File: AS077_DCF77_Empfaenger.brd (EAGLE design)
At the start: 160 x 100 mm, 82 parts, among them IC1 4093N, IC2 4538N, IC3 CA3130E, IC4 4093N, J1 Rückkopplung, J2 JUMPER_J5MM, J3 JUMPER_J5MM, Q1 BF 244A, Q2 BC549C, Q3 BC549, Q4 TRANSISTOR-NPN_BC2385.08, Q5 BC549C, Q6 TRANSISTOR-PNP_BC2145.08, Q7 BC549C

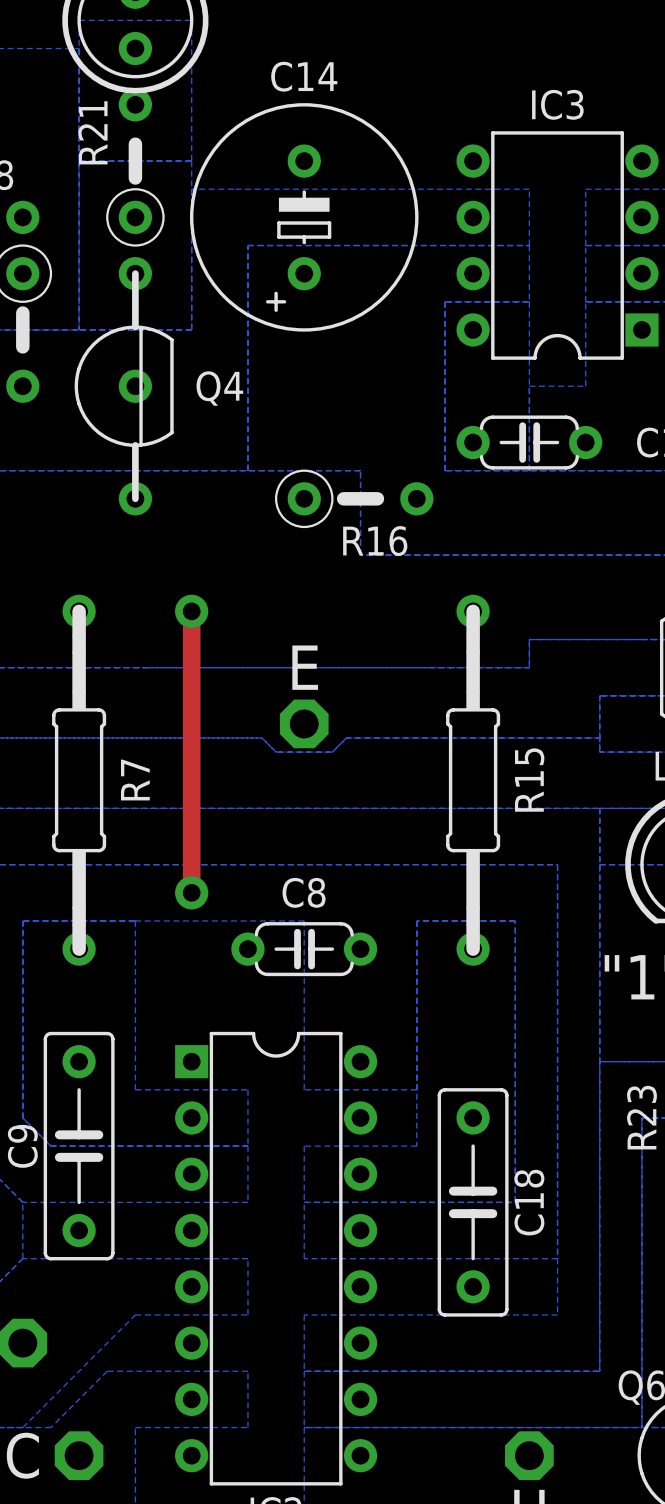
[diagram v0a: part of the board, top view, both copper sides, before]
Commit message: * Added "bottom capacitor" * Added nets and polygons to not connected IC pins
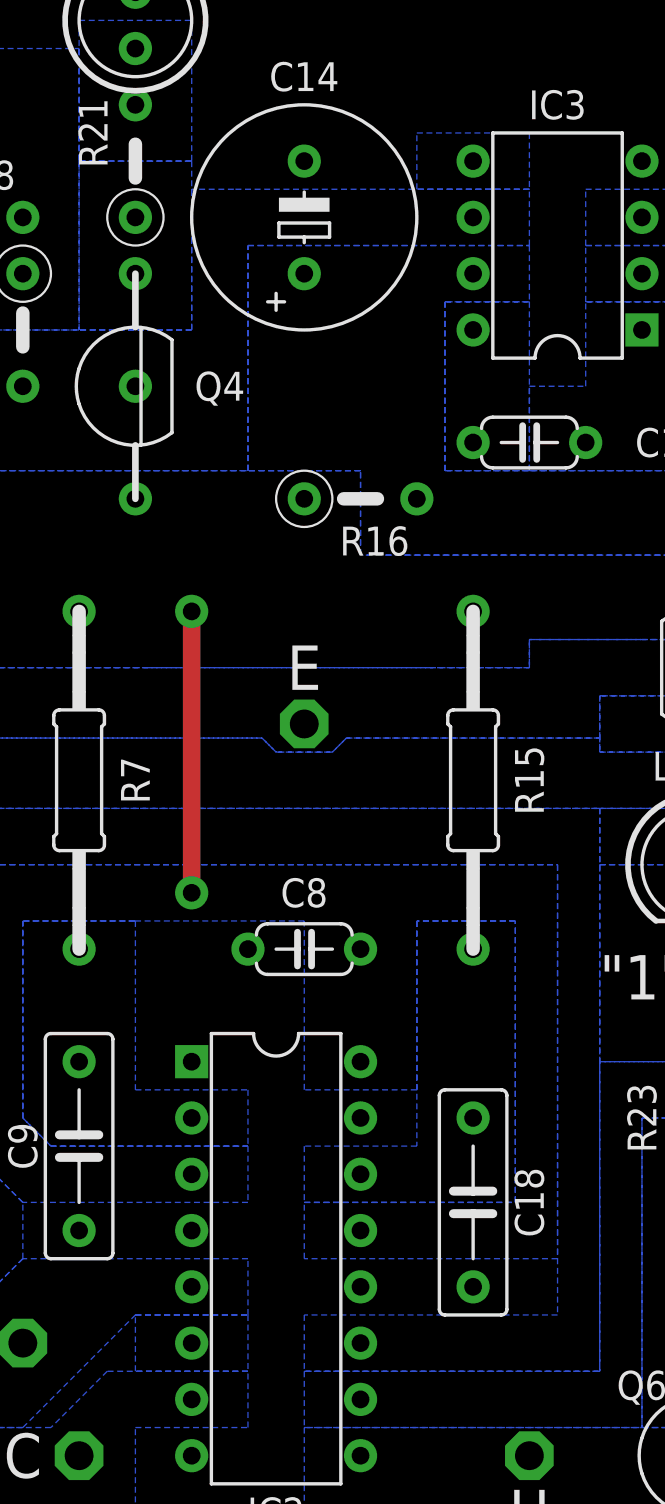
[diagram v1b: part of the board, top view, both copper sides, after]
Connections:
- new net N$45: IC2.6
- new net N$46: IC3.5
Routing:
- added copper zone on layer 16, net N$45
- added copper zone on layer 16, net N$46
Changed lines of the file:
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@@
 <layer number="37" name="tTest" color="7" fill="1" visible="no" active="yes"/>
 <layer number="38" name="bTest" color="7" fill="1" visible="no" active="yes"/>
-<layer number="39" name="tKeepout" color="4" fill="11" visible="no" active="yes"/>
-<layer number="40" name="bKeepout" color="1" fill="11" visible="no" active="yes"/>
-<layer number="41" name="tRestrict" color="4" fill="10" visible="no" active="yes"/>
-<layer number="42" name="bRestrict" color="1" fill="10" visible="no" active="yes"/>
+<layer number="39" name="tKeepout" color="4" fill="11" visible="yes" active="yes"/>
+<layer number="40" name="bKeepout" color="1" fill="11" visible="yes" active="yes"/>
+<layer number="41" name="tRestrict" color="4" fill="10" visible="yes" active="yes"/>
+<layer number="42" name="bRestrict" color="1" fill="10" visible="yes" active="yes"/>
 <layer number="43" name="vRestrict" color="2" fill="10" visible="no" active="yes"/>
 <layer number="44" name="Drills" color="7" fill="1" visible="no" active="yes"/>
-<layer number="45" name="Holes" color="7" fill="1" visible="yes" active="yes"/>
+<layer number="45" name="Holes" color="7" fill="1" visible="no" active="yes"/>
 <layer number="46" name="Milling" color="3" fill="1" visible="no" active="yes"/>
 <layer number="47" name="Measures" color="7" fill="1" visible="no" active="yes"/>
@@
 <text x="142.24" y="27.94" size="3" layer="25" font="vector" ratio="15" align="center">Piezo-
 Element</text>
+<wire x1="129.81" y1="43.815" x2="126.365" y2="43.815" width="0.5" layer="22" style="longdash"/>
+<wire x1="126.365" y1="43.815" x2="125.73" y2="43.18" width="0.5" layer="22" style="longdash" curve="90"/>
+<wire x1="125.73" y1="43.18" x2="125.73" y2="38.1" width="0.5" layer="22" style="longdash"/>
+<wire x1="125.73" y1="38.1" x2="126.365" y2="37.465" width="0.5" layer="22" style="longdash" curve="90"/>
+<wire x1="126.365" y1="37.465" x2="129.81" y2="37.465" width="0.5" layer="22" style="longdash"/>
+<wire x1="129.81" y1="37.465" x2="130.81" y2="38.465" width="0.5" layer="22" style="longdash" curve="90"/>
+<wire x1="130.81" y1="38.465" x2="130.81" y2="42.815" width="0.5" layer="22" style="longdash"/>
+<wire x1="130.81" y1="42.815" x2="129.81" y2="43.815" width="0.5" layer="22" style="longdash" curve="90"/>
+<wire x1="123.19" y1="43.18" x2="125.73" y2="43.18" width="0.3" layer="22"/>
+<wire x1="123.19" y1="38.1" x2="125.73" y2="38.1" width="0.3" layer="22"/>
+<wire x1="129.54" y1="41.275" x2="128.27" y2="41.275" width="0.5" layer="22"/>
+<wire x1="128.27" y1="41.275" x2="127" y2="41.275" width="0.5" layer="22"/>
+<wire x1="129.54" y1="40.005" x2="128.27" y2="40.005" width="0.5" layer="22"/>
+<wire x1="128.27" y1="40.005" x2="127" y2="40.005" width="0.5" layer="22"/>
+<wire x1="128.27" y1="41.275" x2="128.27" y2="42.545" width="0.3" layer="22"/>
+<wire x1="128.27" y1="40.005" x2="128.27" y2="38.735" width="0.3" layer="22"/>
 </plain>
 <attributes>
@@
 <contactref element="R22" pad="1"/>
 </signal>
+<signal name="N$45">
+<contactref element="IC2" pad="6"/>
+<polygon width="0" layer="16" thermals="no">
+<vertex x="43.18" y="19.05"/>
+<vertex x="48.26" y="19.05"/>
+<vertex x="48.26" y="16.51"/>
+<vertex x="43.18" y="16.51"/>
+</polygon>
+</signal>
+<signal name="N$46">
+<contactref element="IC3" pad="5"/>
+<polygon width="0" layer="16" thermals="no">
+<vertex x="55.88" y="72.39"/>
+<vertex x="60.96" y="72.39"/>
+<vertex x="60.96" y="69.85"/>
+<vertex x="55.88" y="69.85"/>
+</polygon>
+</signal>
 </signals>

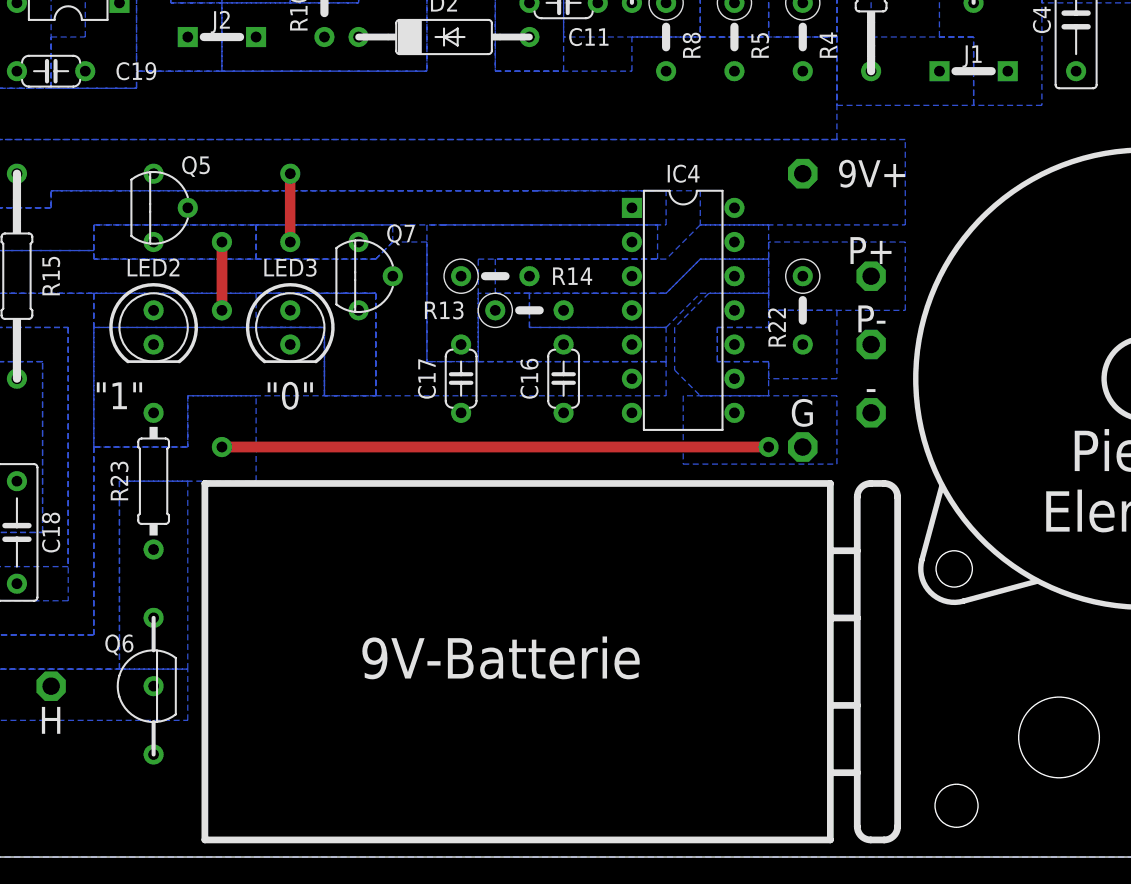
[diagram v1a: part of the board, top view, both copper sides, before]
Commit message: * Added more details to the silkscreen * Fixed all Values in schematic
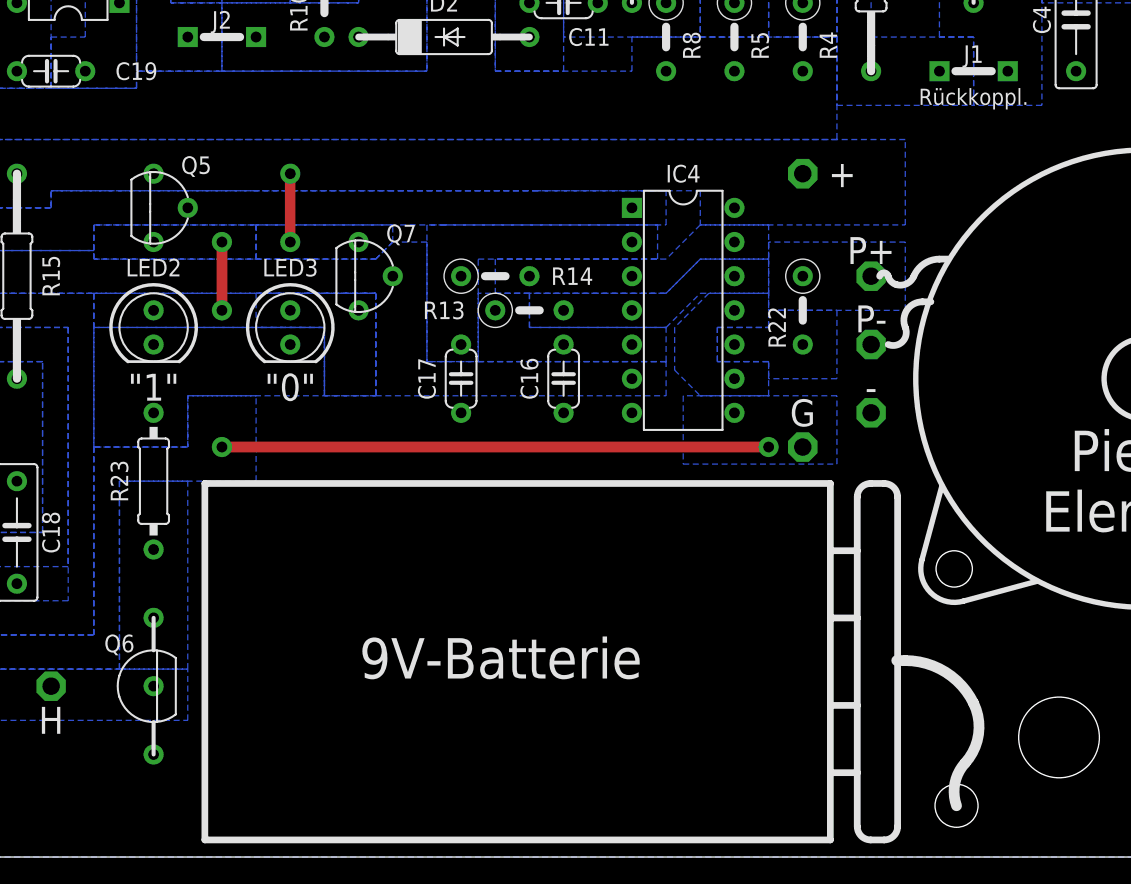
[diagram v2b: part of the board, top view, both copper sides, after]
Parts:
- C1, C14: value (none) -> 470u
- C12, C15: value 270n -> 270n*
- C16, C17: value (none) -> 22n
- C18: value (none) -> 470n*
- C2: value (none) -> 270n*
- C4: value 1n2...2n2 -> 1n2..2n2*
- C8: value (none) -> 100n
- C9: value (none) -> 150n*
- D1, D2: value DIODE_AA112 -> AA112
- LED1: value (none) -> rot
- LED2: value "1" -> rot
- LED3: value "0" -> grün
- Q1: value BF 244A -> BF244A
- Q3: value BC549 -> BC549C
- Q4: value TRANSISTOR-NPN_BC2385.08 -> BC549C
- Q6: value TRANSISTOR-PNP_BC2145.08 -> BC559C
- R1: value (none) -> 39k
- R13: value (none) -> 100k
- R14: value (none) -> 56k
- R19: value 10k (evtl.) -> 10k
- R20: value 1k (evtl.) -> 1k
- R22, R23: value (none) -> 1k
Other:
- board text added: "BAT+"
- board text added: "BAT-"
- board text added: "Rückkoppl."
- board text removed: "9V+"
